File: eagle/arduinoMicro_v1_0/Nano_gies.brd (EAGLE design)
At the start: 71.1 x 59.4 mm, 18 parts, among them Q1 BSS138LT1, Q2 BSS138LT1, Q3 BUZ10

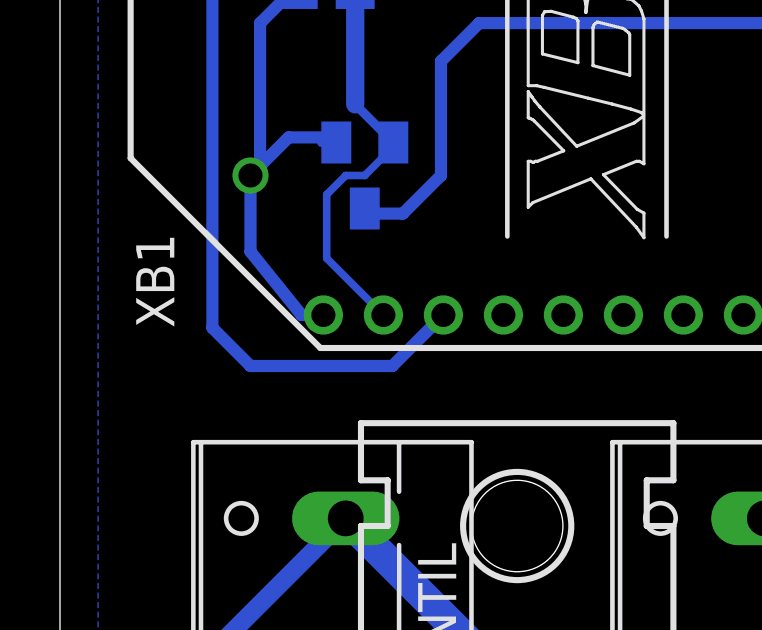
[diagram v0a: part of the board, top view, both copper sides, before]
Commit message: Anpassung eagel Files für Grafiken für die Doku. Bilder in Doku eingefügt
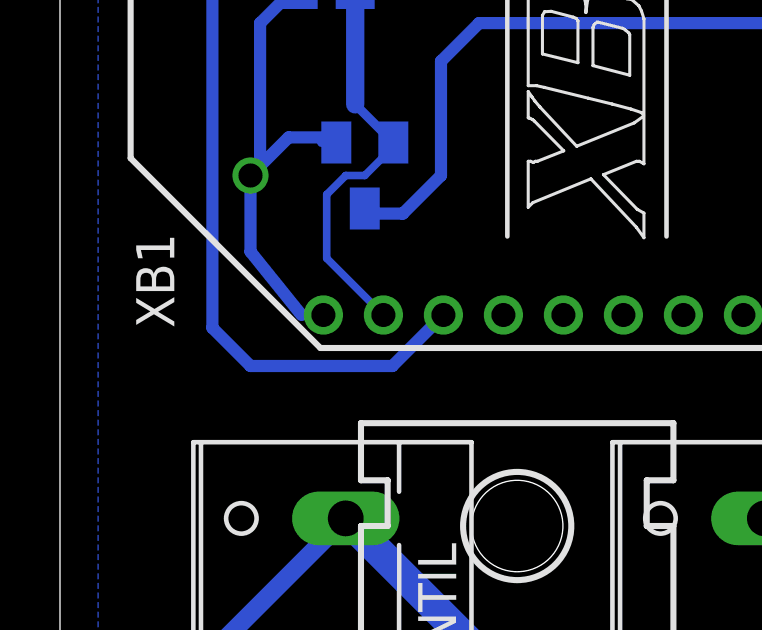
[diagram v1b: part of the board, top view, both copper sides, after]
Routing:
- net +3V3: track 24.3 -> 23.6 mm

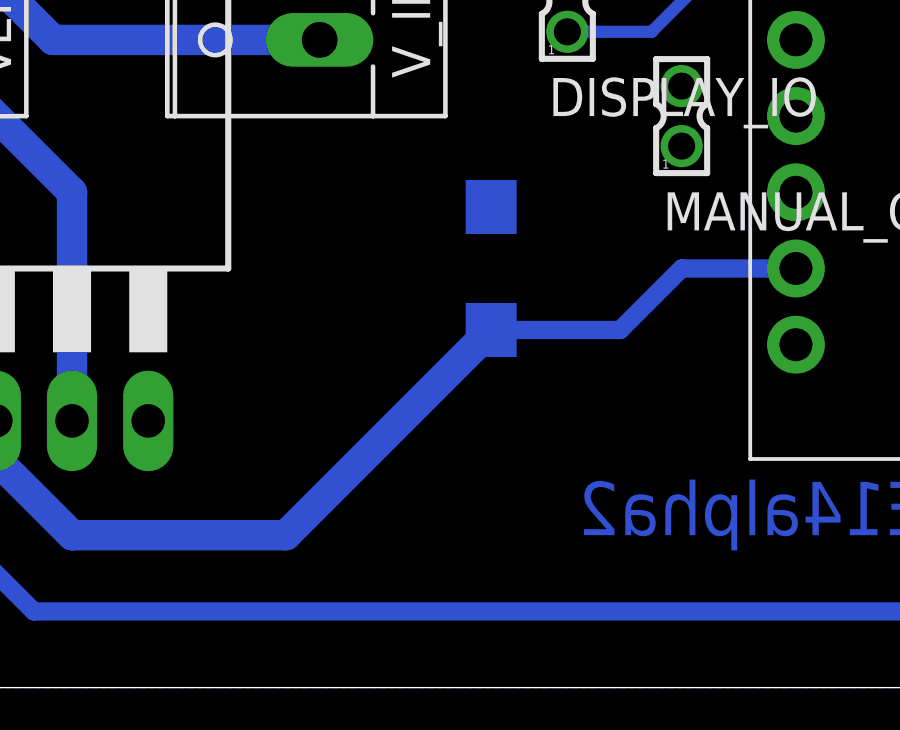
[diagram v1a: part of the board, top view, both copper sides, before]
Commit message: anpassung der Fehler im Schaltplan beim Anschluss XBee zum Mikrocontroller
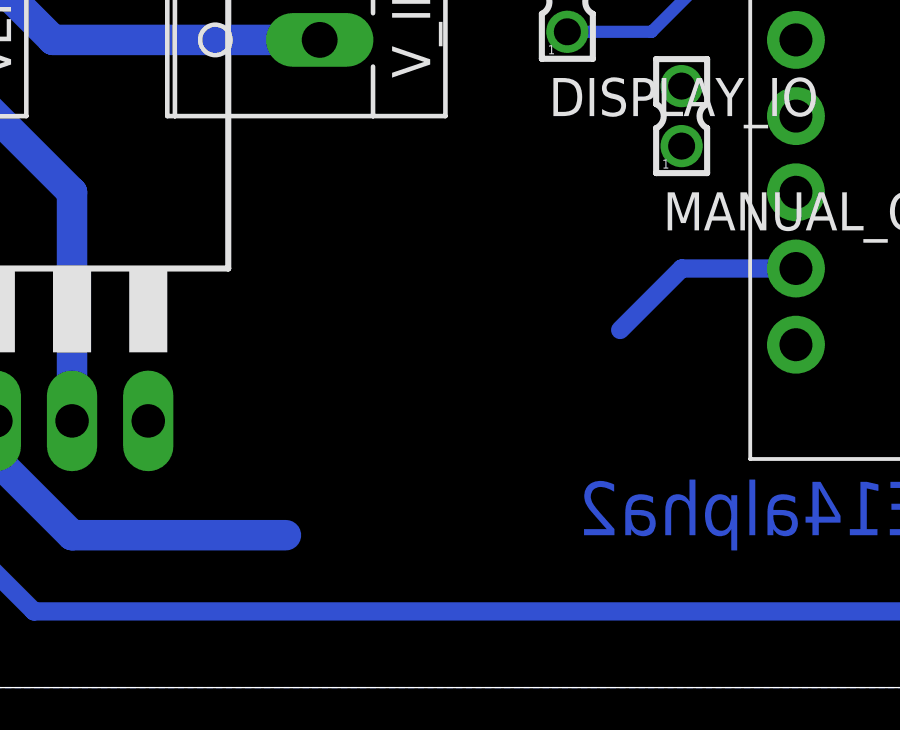
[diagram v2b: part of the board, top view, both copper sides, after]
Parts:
- removed D1: (no value), diode:DO214AC
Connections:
- new net N$1: MANUAL_GIES.2, U$1.P$6
- net GND: no longer D1.A
- net VENTIL_CTRL: no longer D1.C
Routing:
- net VENTIL_CTRL: track 32.7 -> 18.7 mm
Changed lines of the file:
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@@
 <attribute name="OC_FARNELL" value="unknown" x="90.17" y="39.37" size="1.778" layer="27" rot="R270" display="off"/>
 </element>
-<element name="D1" library="diode" package="DO214AC" value="" x="57.15" y="22.86" rot="MR90"/>
 <element name="DISPLAY" library="con-lstb" package="MA04-1" value="" x="60.96" y="41.91" rot="R270">
 <attribute name="OC_NEWARK" value="unknown" x="60.96" y="41.91" size="1.778" layer="27" rot="R270" display="off"/>
@@
 <contactref element="V_IN" pad="2"/>
 <contactref element="Q3" pad="3"/>
-<contactref element="D1" pad="A"/>
 <contactref element="DISPLAY_IO" pad="2"/>
 <contactref element="MANUAL_GIES" pad="1"/>
@@
 <wire x1="86.36" y1="44.18" x2="86.09" y2="44.45" width="0.4064" layer="16"/>
 <wire x1="86.09" y1="44.45" x2="80.01" y2="44.45" width="0.3048" layer="16"/>
+<wire x1="67.31" y1="48.26" x2="80.01" y2="44.45" width="0" layer="19" extent="16-16"/>
+<wire x1="60.96" y1="45.72" x2="67.31" y2="48.26" width="0" layer="19" extent="1-1"/>
+<wire x1="54.72" y1="42.34" x2="60.96" y2="45.72" width="0" layer="19" extent="1-1"/>
+<wire x1="51.435" y1="35.56" x2="54.72" y2="42.34" width="0" layer="19" extent="1-1"/>
+<wire x1="59.69" y1="32.75" x2="51.435" y2="35.56" width="0" layer="19" extent="1-1"/>
+<wire x1="63.5" y1="26.94" x2="59.69" y2="32.75" width="0" layer="19" extent="1-1"/>
+<wire x1="45.72" y1="17.78" x2="51.435" y2="35.56" width="0" layer="19" extent="1-1"/>
 </signal>
 <signal name="BODEN_DIGITAL">
@@
 <signal name="VENTIL_CTRL">
 <contactref element="Q3" pad="1"/>
-<contactref element="D1" pad="C"/>
 <wire x1="40.64" y1="17.78" x2="40.64" y2="16.51" width="1.016" layer="16"/>
 <wire x1="40.64" y1="16.51" x2="43.18" y2="13.97" width="1.016" layer="16"/>
 <wire x1="43.18" y1="13.97" x2="50.31" y2="13.97" width="1.016" layer="16"/>
-<wire x1="50.31" y1="13.97" x2="57.15" y2="20.81" width="1.016" layer="16"/>
 <contactref element="U$1" pad="P$2"/>
-<wire x1="57.15" y1="20.81" x2="61.45" y2="20.81" width="0.6096" layer="16"/>
 <wire x1="61.45" y1="20.81" x2="63.5" y2="22.86" width="0.6096" layer="16"/>
 <wire x1="63.5" y1="22.86" x2="67.31" y2="22.86" width="0.6096" layer="16"/>
+<wire x1="50.31" y1="13.97" x2="61.45" y2="20.81" width="0" layer="19" extent="16-16"/>
 </signal>
 <signal name="N$3">
@@
 <wire x1="81.28" y1="41.91" x2="78.42" y2="41.91" width="0.4064" layer="16"/>
 </signal>
+<signal name="N$1">
+<contactref element="MANUAL_GIES" pad="2"/>
+<contactref element="U$1" pad="P$6"/>
+<wire x1="63.5" y1="28.94" x2="67.31" y2="33.02" width="0" layer="19" extent="1-1"/>
+</signal>
 </signals>
